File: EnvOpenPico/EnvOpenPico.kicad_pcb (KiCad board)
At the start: 2 copper layers, 21.5 x 51.3 mm, 50 parts, among them J2 SKRKAEE020, J3 2.54mm header 01x20, J4 2.54mm header 01x20, J5 Conn_01x03_Male, U1 TLV75533PDBVR, U3 RP2040, Y1 3225_4P

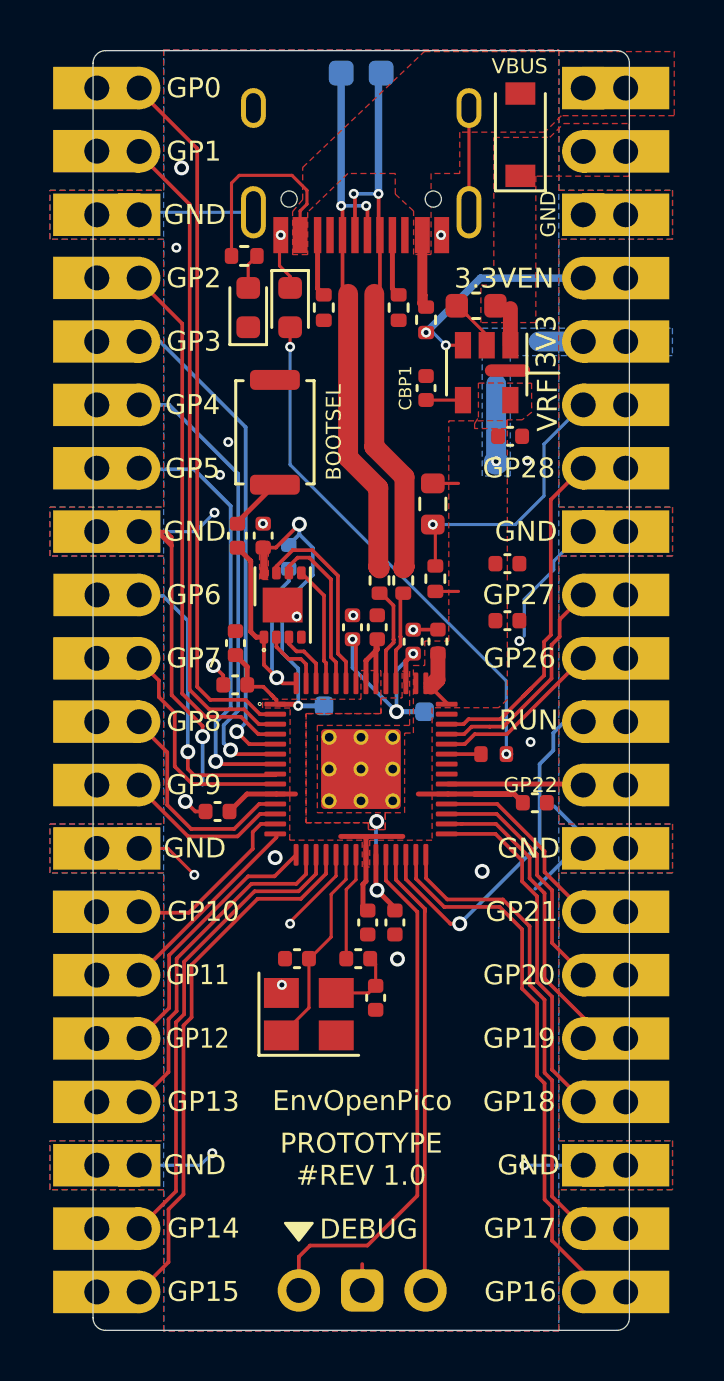
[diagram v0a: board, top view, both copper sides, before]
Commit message: moved some vias off some pads.
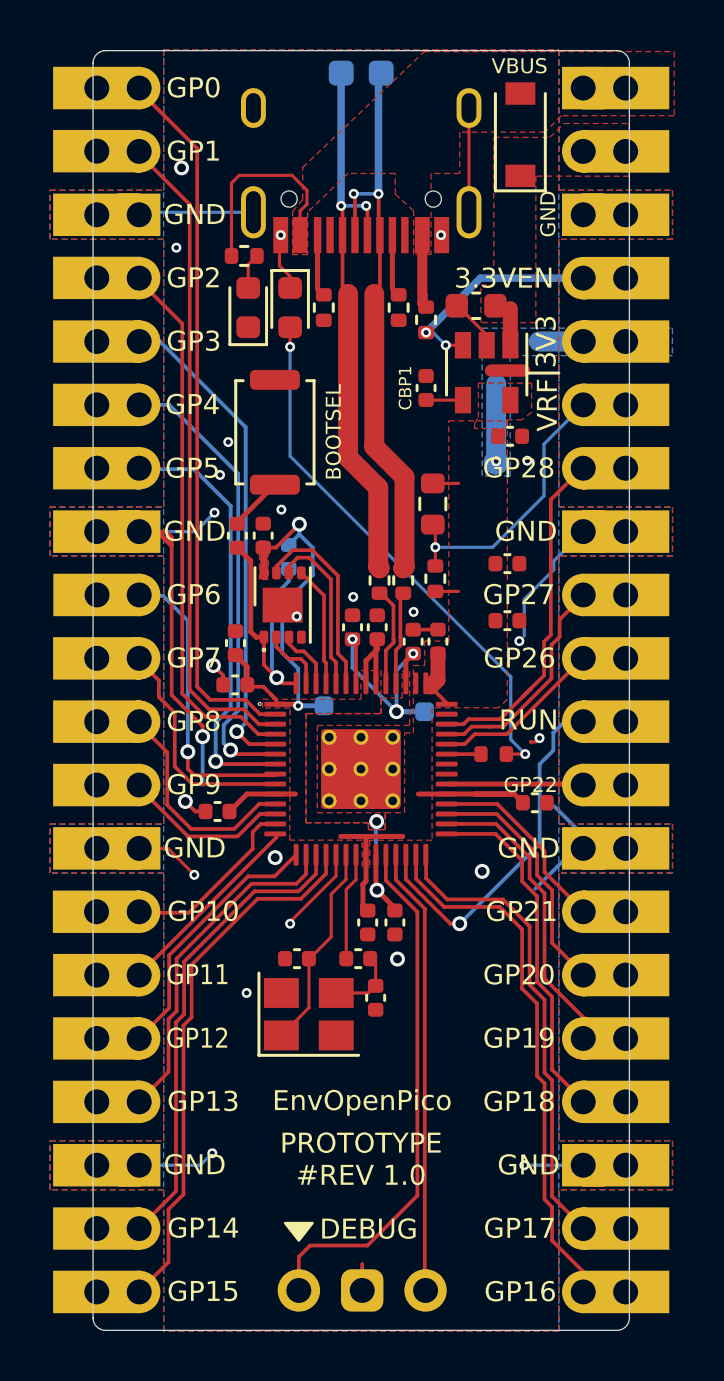
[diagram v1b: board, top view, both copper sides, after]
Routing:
- net Net-(D3-Pad2): track 20.9 -> 21.6 mm

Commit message: corrected some things, it appears GD25Q40 doesnt work with the RP2040 but the GD25Q16/32/64 work fine.
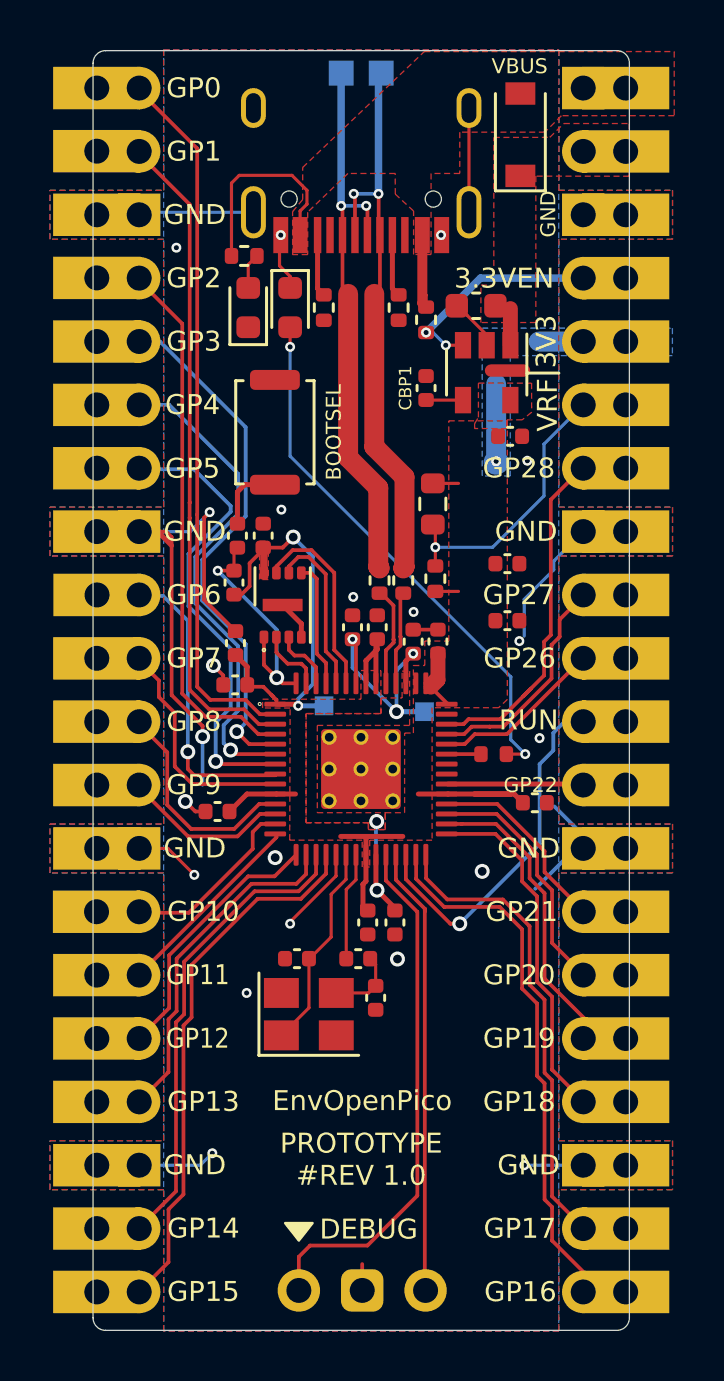
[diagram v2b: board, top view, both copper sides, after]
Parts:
- R2: moved to F.Cu
- moved R2 2.42 mm to (98.5, 78.5), turned to 90 degrees
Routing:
- net GND: track 57.9 -> 65.1 mm, vias 25 -> 21
- net /QSPI_SS: track 11.7 -> 9.63 mm, vias 1 -> 2
- net /GPIO3: track 19.8 -> 21.3 mm
- net /GPIO4: track 18.4 -> 19.9 mm
- net /GPIO5: track 17.3 -> 18.7 mm
- net /~USB_BOOT: track 2.19 -> 2.90 mm
- net +3V3: track 47.5 -> 48.0 mm

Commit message: some small adjustments
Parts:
- removed REF**: Board, kikit:Board
- removed REF** (x2): Tab, kikit:Tab
- added RSW1: Jumper_NO_Small, Button_Switch_SMD:SW_Push_SPST_NO_Alps_SKRK, F.Cu at (107.2, 95.2)
- R12: value 1K 0402 Resistor -> 5.1K 0402 Resistor
- R2: value DNF -> 10K 0402
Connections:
- FLASH1 pad 9: GND -> (no net)
- U3 pad 35: /GPIO23 -> (no net)
- U3 pad 36: /GPIO24 -> (no net)
- U3 pad 41: /GPIO29_ADC3 -> (no net)
- USB1 pad 3: Net-(USB1-Pad3) -> (no net)
- USB1 pad 9: Net-(USB1-Pad9) -> (no net)
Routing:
- net /SWCLK: track 21.3 -> 20.0 mm
- net /RUN: track 14.8 -> 15.8 mm
- net /SWD: track 18.0 -> 18.9 mm
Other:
- board text added: "RESET"

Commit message: added some notes and also various tweaks n what not.
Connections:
- FLASH1 pad 9: (no net) -> GND

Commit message: updated revision to 1.1
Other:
- board text added: "PROTOTYPE #REV 1.1"
- board text removed: "PROTOTYPE #REV 1.0"

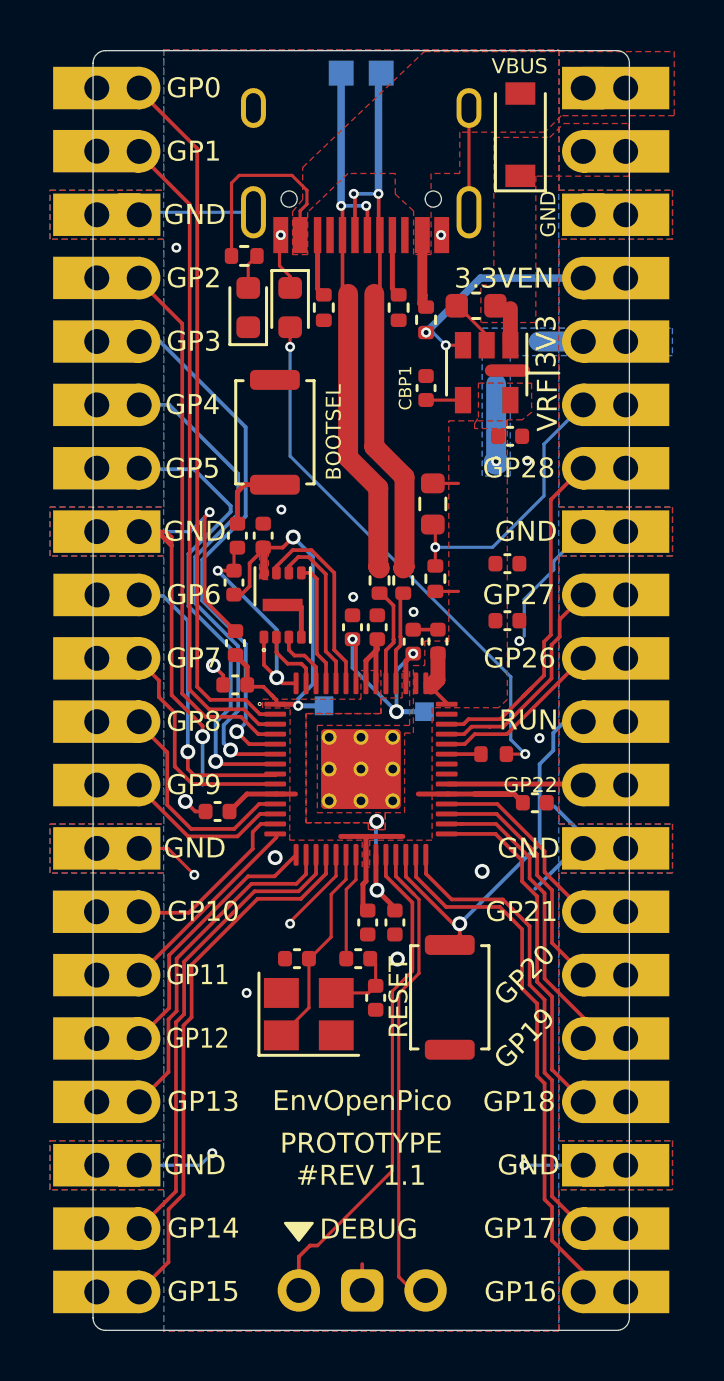
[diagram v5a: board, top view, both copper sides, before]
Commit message: enlarged USB TP Pads and aligned USB port to center.
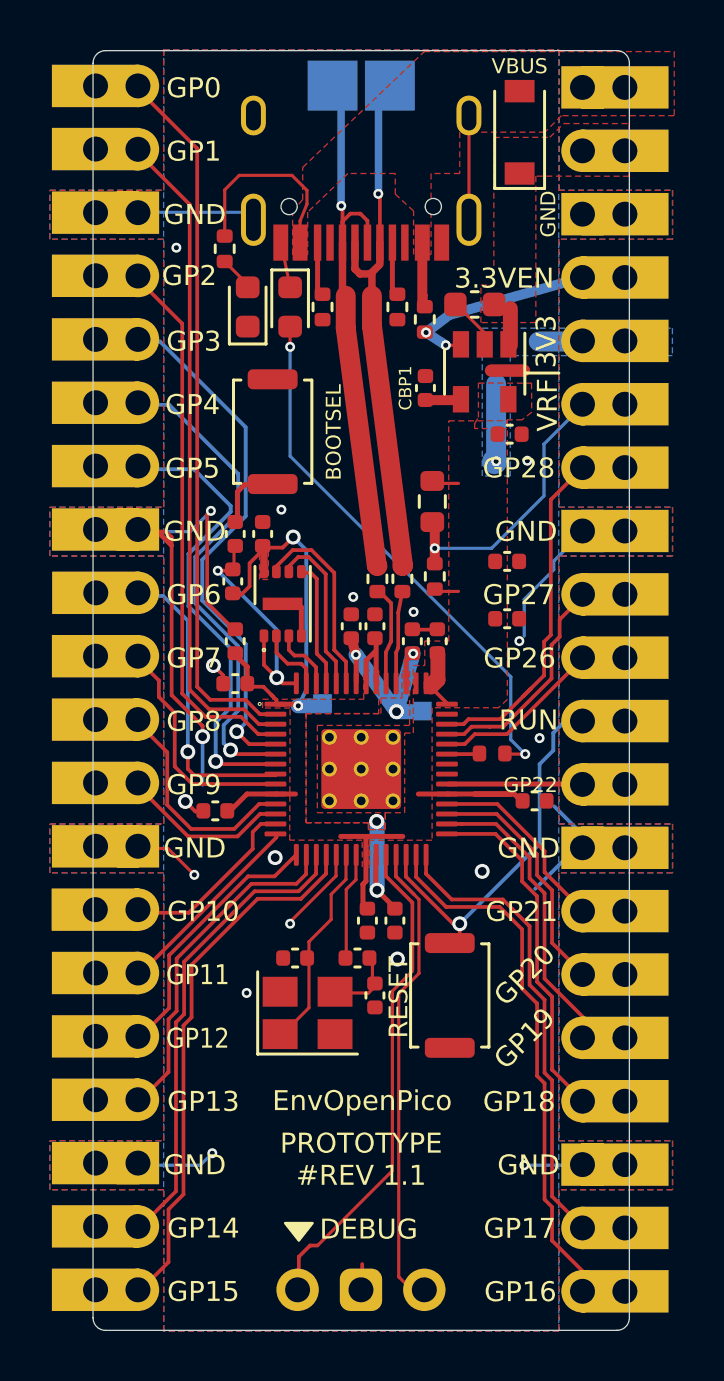
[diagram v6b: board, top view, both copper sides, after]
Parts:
- moved R12 0.83 mm to (98.2, 65.2), turned to 90 degrees
- moved TP2 0.61 mm to (104.8, 58.6)
- moved USB1 0.30 mm to (103.7, 57.2)
- moved TP1 0.13 mm to (102.7, 58.1)
- moved R1 0.11 mm to (98.6, 76.6)
- moved TP8 0.11 mm to (102.1, 83.4)
- moved R3 0.11 mm to (104.3, 78.4)
- moved C8 0.10 mm to (104.2, 80.3)
- moved C19 0.10 mm to (104.2, 95.1)
- moved D1 0.10 mm to (110.0, 60.5)
- moved R9 0.10 mm to (106.5, 75.3)
- moved J3 0.10 mm to (94.7, 106.9)
- moved R10 0.09 mm to (106.6, 78.3)
- moved J2 0.09 mm to (100.1, 72.5)
- moved C17 0.09 mm to (97.8, 87.7)
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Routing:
- net +1V1: track 15.9 -> 17.7 mm
- net USB_D-: track 23.2 -> 22.2 mm, vias 2 -> 1
- net VBUS: track 14.6 -> 13.9 mm
- net +3V3: track 48.0 -> 47.3 mm
- net 3V3_EN: track 9.49 -> 8.94 mm
- net USB_D+: track 22.6 -> 23.0 mm, vias 2 -> 1
- net GND: track 65.4 -> 65.2 mm, vias 21 -> 19
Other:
- board text removed: "DNF"

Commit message: Generated updated Gerber for PCBWAY
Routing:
- net 3V3_EN: track 8.94 -> 10.6 mm
- net +1V1: track 17.7 -> 16.5 mm

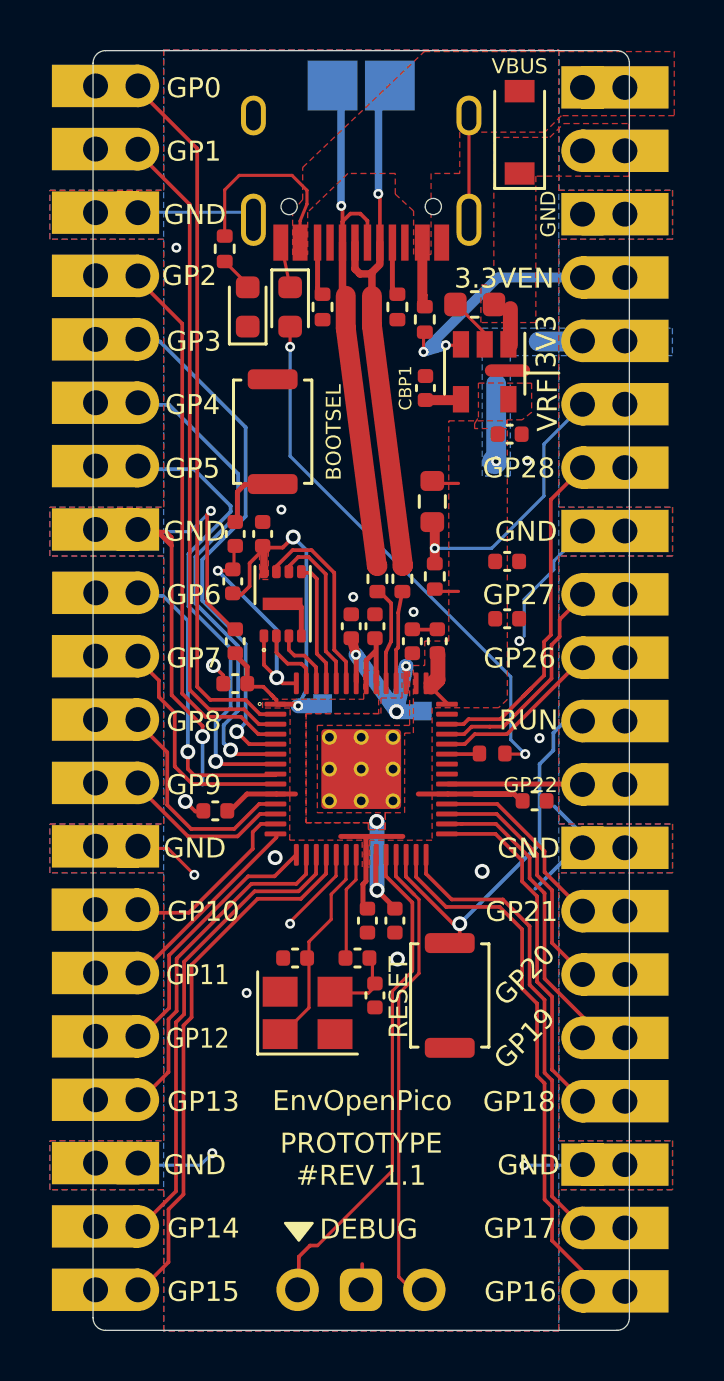
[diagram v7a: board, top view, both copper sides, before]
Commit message: corrected library symbol for reset button
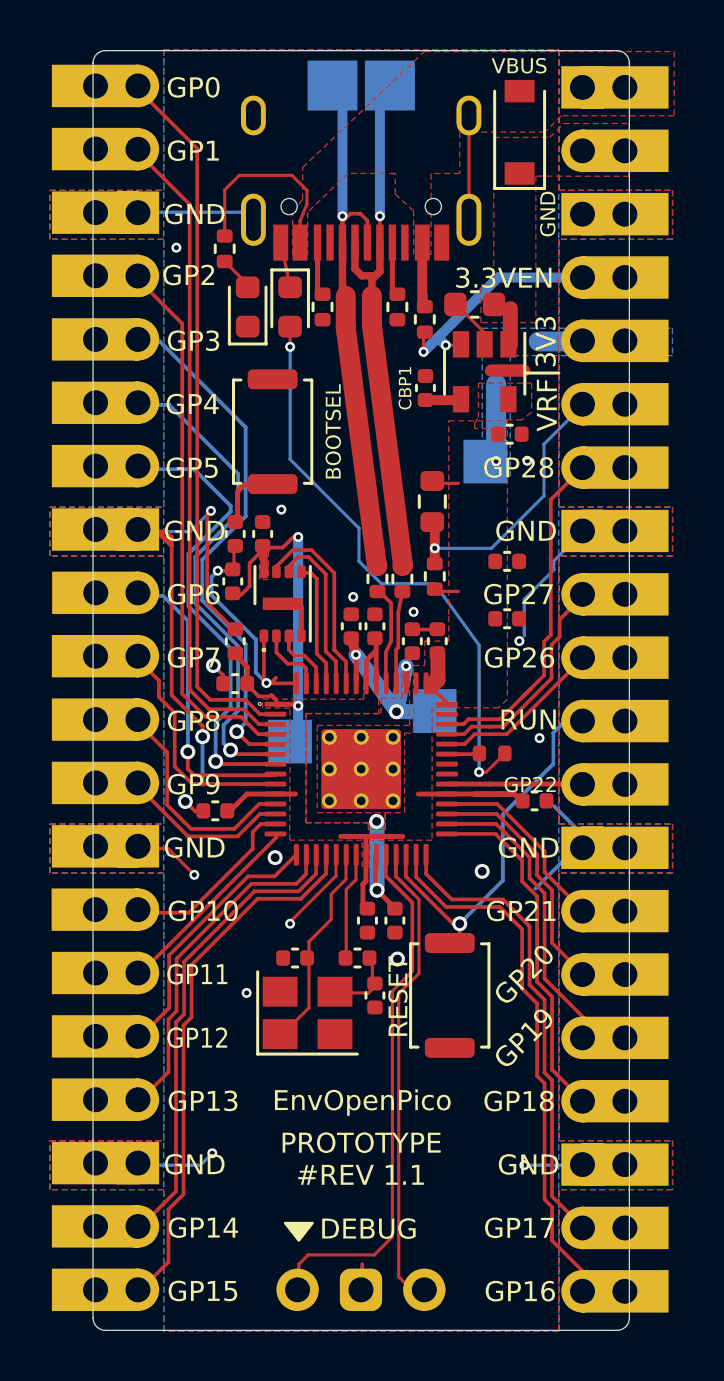
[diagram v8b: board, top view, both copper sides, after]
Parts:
- moved TP8 2.00 mm to (100.8, 84.9)
- moved TP7 0.50 mm to (106.6, 83.7)
- moved TP6 0.38 mm to (108.6, 73.7)
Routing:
- net Net-(D3-Pad2): track 21.8 -> 23.4 mm
- net /SWCLK: track 20.0 -> 21.3 mm
- net /QSPI_SS: track 9.63 -> 10.7 mm
